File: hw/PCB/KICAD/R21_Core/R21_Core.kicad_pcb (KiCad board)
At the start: 2 copper layers, 42.4 x 45.9 mm, 221 parts, among them J1 JTAGICE3-10p, Q1 MOSFET_N, SW1 SPST_SW, T1 TPS61089RNR, U1 SAMR21E, U10 USB2, U11 AP2112K, U2 AP2112K, U3 LSM9DS1, U4 TPS2559-Q1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

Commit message: Lots of changes- firmware, board rev, mods
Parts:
- removed the REF** at (103.1, 108.0)
- removed the REF** at (107.0, 133.3)
- removed the REF** at (96.0, 95.3)
- moved C19 0.25 mm to (108.1, 110.4)
- moved L2 0.25 mm to (106.9, 106.3)
- moved C25 0.15 mm to (106.1, 108.8)
- moved C31 0.09 mm to (96.3, 129.5)
- turned D1 to 270 degrees
- turned D2 to 270 degrees
- turned D3 to 270 degrees
- turned D5 to 270 degrees
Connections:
- D1 pad 1: Net-(D1-Pad1) -> GND
- D1 pad 2: GND -> Net-(D1-Pad2)
- D2 pad 1: Net-(D2-Pad1) -> BB_GND
- D2 pad 2: BB_GND -> Net-(D2-Pad2)
- D3 pad 1: Net-(D3-Pad1) -> BB_GND
- D3 pad 2: BB_GND -> Net-(D3-Pad2)
- Q1 pad D: Net-(D5-Pad2) -> Net-(D5-Pad1)
- R1 pad 1: Net-(D1-Pad1) -> Net-(D1-Pad2)
- R12 pad 1: Net-(D5-Pad1) -> Net-(D5-Pad2)
- R2 pad 1: Net-(D2-Pad1) -> Net-(D2-Pad2)
- R9 pad 1: Net-(D3-Pad1) -> Net-(D3-Pad2)
- U3 pad 2: SDA_LV -> SCL_LV
- U3 pad 4: SCL_LV -> SDA_LV
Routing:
- net BB_GND: track 81.2 -> 83.9 mm
- net Net-(D3-Pad2): track 0.00 -> 2.19 mm
- net Net-(D3-Pad1): track 2.19 -> 0.00 mm
- net Net-(D2-Pad2): track 0.00 -> 2.19 mm
- net Net-(D2-Pad1): track 2.19 -> 0.00 mm
- net GND: track 69.5 -> 71.2 mm
- net +3V3: track 62.9 -> 64.1 mm
- net Net-(D1-Pad2): track 0.00 -> 1.16 mm
- net Net-(D1-Pad1): track 1.16 -> 0.00 mm
- net Net-(A1-Pad1): track 8.37 -> 9.18 mm
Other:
- outline, holes or cut-outs redrawn

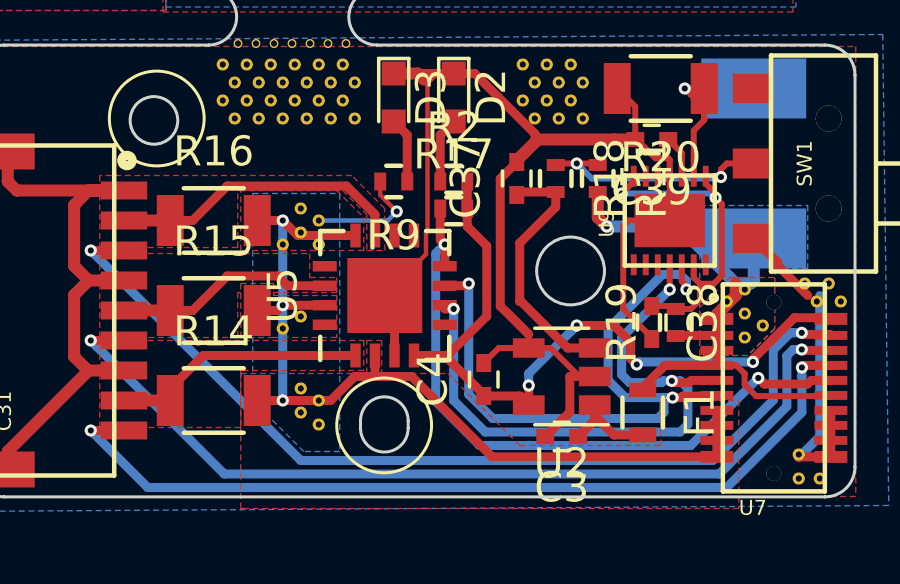
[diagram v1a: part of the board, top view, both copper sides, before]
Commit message: Added addendum to boards, modules for debug, comms description
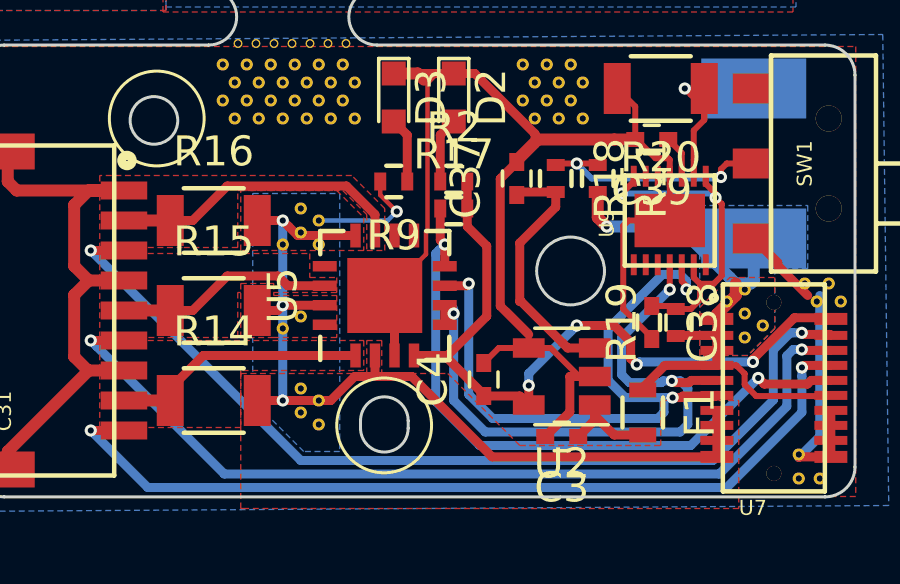
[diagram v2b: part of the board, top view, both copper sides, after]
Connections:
- U5 pad 5: Net-(U5-Pad5) -> BB_SCL
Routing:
- net BB_SCL: track 21.3 -> 22.1 mm

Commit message: ...I forgot to commit for a while
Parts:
- added REF**: BreakawayHole, 0.0625hole, F.Cu at (107.0, 133.2)
- added REF**: BreakawayHole, 0.0625hole, F.Cu at (103.2, 108.0)
- added REF**: BreakawayHole, 0.0625hole, F.Cu at (96.0, 95.3)
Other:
- outline, holes or cut-outs redrawn
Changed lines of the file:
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@@
   (general
     (links 384)
-    (no_connects 1)
-    (area 80.247629 89.728439 122.717252 135.763344)
+    (no_connects 0)
+    (area 78.092857 85.795238 126.700001 140.125)
     (thickness 1.6)
-    (drawings 84)
-    (tracks 1285)
+    (drawings 72)
+    (tracks 1288)
     (zones 0)
-    (modules 218)
+    (modules 221)
     (nets 132)
   )
@@
   )
   (setup
-    (last_trace_width 0.3)
+    (last_trace_width 0.15)
     (user_trace_width 0.2)
     (user_trace_width 0.3)
@@
     (mod_text_size 1 1)
     (mod_text_width 0.15)
-    (pad_size 0.4064 0.4064)
-    (pad_drill 0.2032)
+    (pad_size 2.26 2.26)
+    (pad_drill 2.26)
     (pad_to_mask_clearance 0.2)
     (aux_axis_origin 0 0)
@@
     (add_net ~FAULT~)
   )
+  (module 0.0625hole (layer F.Cu)
+    (at 106.979288 133.188885)
+    (fp_text reference REF** (at 0 1.5) (layer F.SilkS) hide
+      (effects (font (size 0.127 0.127) (thickness 0.03175)))
+    )
+    (fp_text value BreakawayHole (at 0 -1.5) (layer F.Fab) hide
+      (effects (font (size 0.127 0.127) (thickness 0.03175)))
+    )
+    (pad "" np_thru_hole circle (at 0.036087 0.008552 180) (size 1.6 1.6) (drill 1.5875) (layers *.Cu *.Mask))
+  )
+  (module 0.0625hole (layer F.Cu)
+    (at 103.248087 107.987752)
+    (fp_text reference REF** (at 0 1.5) (layer F.SilkS) hide
+      (effects (font (size 0.127 0.127) (thickness 0.03175)))
+    )
+    (fp_text value BreakawayHole (at 0 -1.5) (layer F.Fab) hide
+      (effects (font (size 0.127 0.127) (thickness 0.03175)))
+    )
+    (pad "" np_thru_hole circle (at 0.036087 0.008552 180) (size 1.6 1.6) (drill 1.5875) (layers *.Cu *.Mask))
+  )
+  (module 0.0625hole (layer F.Cu)
+    (at 96.006942 95.337752)
+    (fp_text reference REF** (at 0 1.5) (layer F.SilkS) hide
+      (effects (font (size 0.127 0.127) (thickness 0.03175)))
+    )
+    (fp_text value BreakawayHole (at 0 -1.5) (layer F.Fab) hide
+      (effects (font (size 0.127 0.127) (thickness 0.03175)))
+    )
+    (pad "" np_thru_hole circle (at 0.003942 -0.071448 180) (size 1.6 1.6) (drill 1.5875) (layers *.Cu *.Mask))
+  )
   (module _CSL:stitchingVia (layer F.Cu)
     (at 92.3 114.4 180)
@@
     (pad "" np_thru_hole circle (at 0 0) (size 0.3 0.3) (drill 0.2032) (layers *.Cu *.Mask))
   )
-  (gr_arc (start 106.979288 133.425) (end 107.773038 133.425) (angle 180) (layer Edge.Cuts) (width 0.1))
-  (gr_line (start 106.185538 133.171) (end 106.185538 133.425) (layer Edge.Cuts) (width 0.1))
-  (gr_arc (start 106.979288 133.171) (end 106.185538 133.171) (angle 180) (layer Edge.Cuts) (width 0.1))
-  (gr_line (start 107.773038 133.171) (end 107.773038 133.425) (layer Edge.Cuts) (width 0.1))
-  (gr_arc (start 102.975 107.987752) (end 102.975 108.781502) (angle 180) (layer Edge.Cuts) (width 0.1))
-  (gr_line (start 103.229 108.781502) (end 102.975 108.781502) (layer Edge.Cuts) (width 0.1))
-  (gr_arc (start 103.229 107.987752) (end 103.229 107.194002) (angle 180) (layer Edge.Cuts) (width 0.1))
-  (gr_line (start 103.229 107.194002) (end 102.975 107.194002) (layer Edge.Cuts) (width 0.1))
-  (gr_line (start 96.217 96.131502) (end 95.963 96.131502) (layer Edge.Cuts) (width 0.1))
-  (gr_line (start 96.217 94.544002) (end 95.963 94.544002) (layer Edge.Cuts) (width 0.1))
-  (gr_arc (start 96.217 95.337752) (end 96.217 94.544002) (angle 180) (layer Edge.Cuts) (width 0.1))
-  (gr_arc (start 95.963 95.337752) (end 95.963 96.131502) (angle 180) (layer Edge.Cuts) (width 0.1))
   (gr_arc (start 85.856942 95.337752) (end 90.54232 92.345565) (angle -166.9887828) (layer Edge.Cuts) (width 0.1))
   (gr_arc (start 103.111087 107.987752) (end 100.72363 106.184081) (angle -37.07023682) (layer Edge.Cuts) (width 0.1))
@@
   (segment (start 87.505895 103.726338) (end 87.262002 103.726338) (width 0.2) (layer F.Cu) (net 5))
   (segment (start 87.262002 103.726338) (end 86.7 104.28834) (width 0.2) (layer F.Cu) (net 5))
+  (segment (start 85.915 110.625) (end 85.915 110.565) (width 0.15) (layer F.Cu) (net 7))
+  (segment (start 85.915 110.565) (end 86.08 110.4) (width 0.15) (layer F.Cu) (net 7))
+  (segment (start 86.08 110.4) (end 86.08 110.3) (width 0.15) (layer F.Cu) (net 7))
   (segment (start 87.606262 109.453) (end 87.708 109.453) (width 0.2) (layer F.Cu) (net 7))
   (segment (start 87.708 109.453) (end 88.117738 109.453) (width 0.2) (layer F.Cu) (net 7))
